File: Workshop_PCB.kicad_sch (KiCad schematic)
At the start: 15 parts, among them J1 Conn_01x04, SW1 SW_MEC_5E, U1 STM32F042C6Tx, U2 AMS1117-3.3

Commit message: Finish schematic, assign components and footprints
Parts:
- removed SW1: SW_MEC_5E, symbol Switch:SW_MEC_5E
- added D2: LED, LED_SMD:LED_0805_2012Metric, symbol Device:LED
- added J2: USB_C_Receptacle_USB2.0_16P, Connector_USB:USB_C_Receptacle_GCT_USB4105-xx-A_16P_TopMnt_Horizontal, symbol Connector:USB_C_Receptacle_USB2.0_16P
- added J3, J4: Conn_01x22, Connector_PinSocket_2.54mm:PinSocket_1x22_P2.54mm_Vertical, symbol Connector_Generic:Conn_01x22
- added R3, R4: 5.1k, Resistor_SMD:R_0603_1608Metric, symbol Device:R
- added R5: 50R, Resistor_SMD:R_0603_1608Metric, symbol Device:R
- added SW1: SW_Push, Button_Switch_SMD:SW_Push_1P1T_XKB_TS-1187A, symbol Switch:SW_Push
- added U3: USBLC6-2SC6, Package_TO_SOT_SMD:SOT-23-6, symbol Power_Protection:USBLC6-2SC6
- C1, C2, C3, C4, C5, C6, C7, C8: footprint (none) -> Capacitor_SMD:C_0603_1608Metric
- D1: footprint (none) -> LED_SMD:LED_0805_2012Metric; LCSC (none) -> C2297
- J1: footprint (none) -> Connector_PinSocket_2.54mm:PinSocket_1x04_P2.54mm_Horizontal
- R1: footprint (none) -> Resistor_SMD:R_0603_1608Metric
- R2: value R -> 220R; footprint (none) -> Resistor_SMD:R_0603_1608Metric
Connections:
- net +3V3: now also J3.5 (Pin_5)
- net +5V: now also J2.A4 (VBUS), J2.A9 (VBUS), J2.B4 (VBUS), J2.B9 (VBUS), J3.21 (Pin_21), J3.22 (Pin_22), U3.5 (VBUS)
- net A0: now also J3.7 (Pin_7)
- net A1: now also J3.8 (Pin_8)
- net A2: now also J3.9 (Pin_9)
- net A3: now also J3.10 (Pin_10)
- net A4: now also J3.11 (Pin_11)
- net A5: now also J3.12 (Pin_12)
- net A6: now also J3.13 (Pin_13)
- net A7: now also J3.14 (Pin_14)
- net A8: now also J3.15 (Pin_15)
- net A9: now also J3.16 (Pin_16)
- net BOOT: now also J3.19 (Pin_19)
- net CAN_RX_PWM_D18: now also J4.2 (Pin_2)
- net CAN_TX_PWM_D19: now also J4.1 (Pin_1)
- net D16: now also J4.4 (Pin_4)
- net D17: now also J4.3 (Pin_3)
- net D2: now also J4.20 (Pin_20)
- net D20: now also J3.1 (Pin_1)
- net D21: now also J3.2 (Pin_2)
- net D22: now also J3.3 (Pin_3)
- net D23: now also J3.4 (Pin_4)
- net D24: now also D2.2 (A)
- net D5: now also J4.17 (Pin_17)
- net D6: now also J4.16 (Pin_16)
- net D7: now also J4.14 (Pin_14)
- net D8: now also J4.13 (Pin_13)
- net GND: now also J2.A1 (GND), J2.A12 (GND), J2.B1 (GND), J2.B12 (GND), J2.S1 (SHIELD), J3.17 (Pin_17), J3.18 (Pin_18), R3.1, R4.1, R5.2, SW1.1, U3.2 (GND)
- net I2C_SCL_PWM_D3: now also J4.19 (Pin_19)
- net I2C_SDA_PWM_D4: now also J4.18 (Pin_18)
- net I2S_WS_PWM_D12: now also J4.9 (Pin_9)
- net PWM_D9: now also J4.12 (Pin_12)
- net SPI_MISO_I2S_MCK_PWM_D14: now also J4.6 (Pin_6)
- net SPI_MOSI_I2S_SD_PWM_D15: now also J4.5 (Pin_5)
- net SPI_SCK_PWM_D13: now also J4.8 (Pin_8)
- net USART_TX_PWM_D10: now also J4.11 (Pin_11)
- net USART_TX_PWM_D11: now also J4.10 (Pin_10)
- net USB_DM_D0: now also J4.22 (Pin_22), U3.6 (I/O1)
- net USB_DP_D1: now also J4.21 (Pin_21), U3.4 (I/O2)
- net NRST: now reaches C1.2, U1.7 (NRST)
- net NRST: now also J3.20 (Pin_20), SW1.2
- new net: D2.1 (K), R5.1
- new net: J2.B5 (CC2), R4.2
- new net: J2.A5 (CC1), R3.2
- new net: J2.A6 (D+), J2.B6 (D+), U3.3 (I/O2)
- new net: J2.A7 (D-), J2.B7 (D-), U3.1 (I/O1)
- no-connect marks 0 -> 5
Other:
- title: (none) -> Hackpill
- moved on the sheet: C1, C2, C3, C4, C5, C6, C7, C8, J1, R1, U1, U2

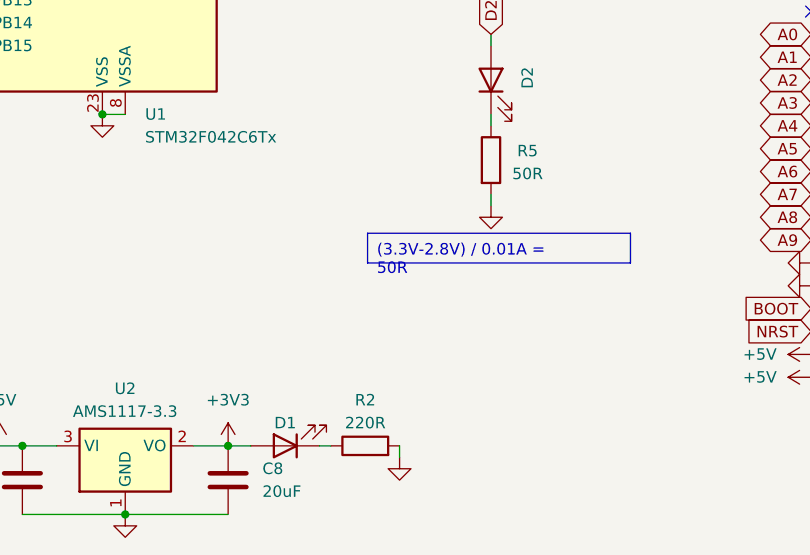
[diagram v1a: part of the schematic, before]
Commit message: Finish component selection and footprint assignment
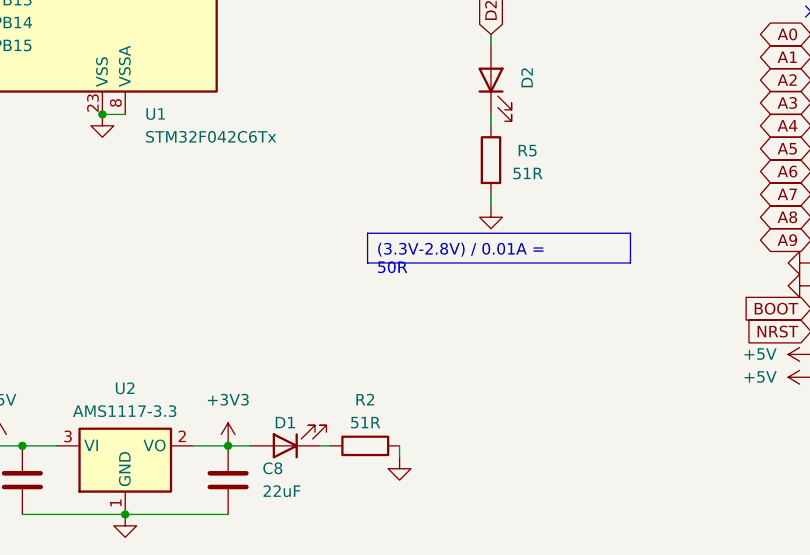
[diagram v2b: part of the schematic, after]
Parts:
- C8: value 20uF -> 22uF
- J2: footprint Connector_USB:USB_C_Receptacle_GCT_USB4105-xx-A_16P_TopMnt_Horizontal -> Connector_USB:USB_C_Receptacle_Hanbo_16P_TopMnt_Horizontal; LCSC (none) -> C6332269
- R2: value 220R -> 51R
- R5: value 50R -> 51R
- SW1: LCSC (none) -> C318884
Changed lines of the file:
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@@
 			)
 		)
-		(property "Value" "20uF"
+		(property "Value" "22uF"
 			(at 115.57 163.8299 0)
 			(effects
@@
 			)
 		)
-		(property "Footprint" "Connector_USB:USB_C_Receptacle_GCT_USB4105-xx-A_16P_TopMnt_Horizontal"
+		(property "Footprint" "Connector_USB:USB_C_Receptacle_Hanbo_16P_TopMnt_Horizontal"
 			(at 203.2 60.96 0)
 			(effects
@@
 			)
 		)
+		(property "LCSC" "C6332269"
+			(at 199.39 60.96 0)
+			(effects
+				(font
+					(size 1.27 1.27)
+				)
+				(hide yes)
+			)
+		)
 		(pin "B7"
 		)
@@
 		)
 		(property "Description" "Push button switch, generic, two pins"
+			(at 64.77 50.8 0)
+			(effects
+				(font
+					(size 1.27 1.27)
+				)
+				(hide yes)
+			)
+		)
+		(property "LCSC" "C318884"
 			(at 64.77 50.8 0)
 			(effects
@@
 			)
 		)
-		(property "Value" "220R"
+		(property "Value" "51R"
 			(at 127 156.21 90)
 			(effects
@@
 			)
 		)
-		(property "Value" "50R"
+		(property "Value" "51R"
 			(at 145.034 128.524 0)
 			(effects

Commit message: Start tracing board
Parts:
- J1: footprint Connector_PinSocket_2.54mm:PinSocket_1x04_P2.54mm_Horizontal -> Connector_PinSocket_2.54mm:PinSocket_1x04_P2.54mm_Vertical
- J3, J4: LCSC C2765186 -> (none)
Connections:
- net A0: now also U1.10 (PA0); no longer U1.19 (PB1)
- net A1: now also U1.11 (PA1); no longer U1.18 (PB0)
- net A2: now also U1.12 (PA2); no longer U1.17 (PA7)
- net A3: now also U1.13 (PA3); no longer U1.16 (PA6)
- net A4: now also U1.14 (PA4); no longer U1.15 (PA5)
- net A5: now also U1.15 (PA5); no longer U1.14 (PA4)
- net A6: now also U1.16 (PA6); no longer U1.13 (PA3)
- net A7: now also U1.17 (PA7); no longer U1.12 (PA2)
- net A8: now also U1.18 (PB0); no longer U1.11 (PA1)
- net A9: now also U1.19 (PB1); no longer U1.10 (PA0)
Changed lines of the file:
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@@
 		)
 	)
-	(global_label "A8"
+	(global_label "A1"
 		(shape bidirectional)
 		(at 113.03 53.34 0)
@@
 		)
 	)
-	(global_label "A6"
+	(global_label "A3"
 		(shape bidirectional)
 		(at 113.03 58.42 0)
@@
 		)
 	)
-	(global_label "A2"
+	(global_label "A7"
 		(shape bidirectional)
 		(at 113.03 68.58 0)
@@
 		)
 	)
-	(global_label "A5"
+	(global_label "A4"
 		(shape bidirectional)
 		(at 113.03 60.96 0)
@@
 		)
 	)
-	(global_label "A9"
+	(global_label "A0"
 		(shape bidirectional)
 		(at 113.03 50.8 0)
@@
 		)
 	)
-	(global_label "A1"
+	(global_label "A8"
 		(shape bidirectional)
 		(at 82.55 76.2 180)
@@
 		)
 	)
-	(global_label "A3"
+	(global_label "A6"
 		(shape bidirectional)
 		(at 113.03 66.04 0)
@@
 		)
 	)
-	(global_label "A4"
+	(global_label "A5"
 		(shape bidirectional)
 		(at 113.03 63.5 0)
@@
 		)
 	)
-	(global_label "A0"
+	(global_label "A9"
 		(shape bidirectional)
 		(at 82.55 78.74 180)
@@
 		)
 	)
-	(global_label "A7"
+	(global_label "A2"
 		(shape bidirectional)
 		(at 113.03 55.88 0)
@@
 			)
 		)
-		(property "Footprint" "Connector_PinSocket_2.54mm:PinSocket_1x04_P2.54mm_Horizontal"
+		(property "Footprint" "Connector_PinSocket_2.54mm:PinSocket_1x04_P2.54mm_Vertical"
 			(at 142.24 83.82 0)
 			(effects
@@
 			)
 		)
-		(property "LCSC" "C2765186"
+		(property "LCSC" ""
 			(at 186.69 123.19 0)
 			(effects
@@
 			)
 		)
-		(property "LCSC" "C2765186"
+		(property "LCSC" ""
 			(at 181.61 123.19 0)
 			(effects

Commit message: Finish PCB
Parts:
- J1: footprint Connector_PinSocket_2.54mm:PinSocket_1x04_P2.54mm_Vertical -> Connector_PinHeader_2.54mm:PinHeader_1x04_P2.54mm_Vertical
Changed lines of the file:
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@@
 			)
 		)
-		(property "Footprint" "Connector_PinSocket_2.54mm:PinSocket_1x04_P2.54mm_Vertical"
+		(property "Footprint" "Connector_PinHeader_2.54mm:PinHeader_1x04_P2.54mm_Vertical"
 			(at 142.24 83.82 0)
 			(effects

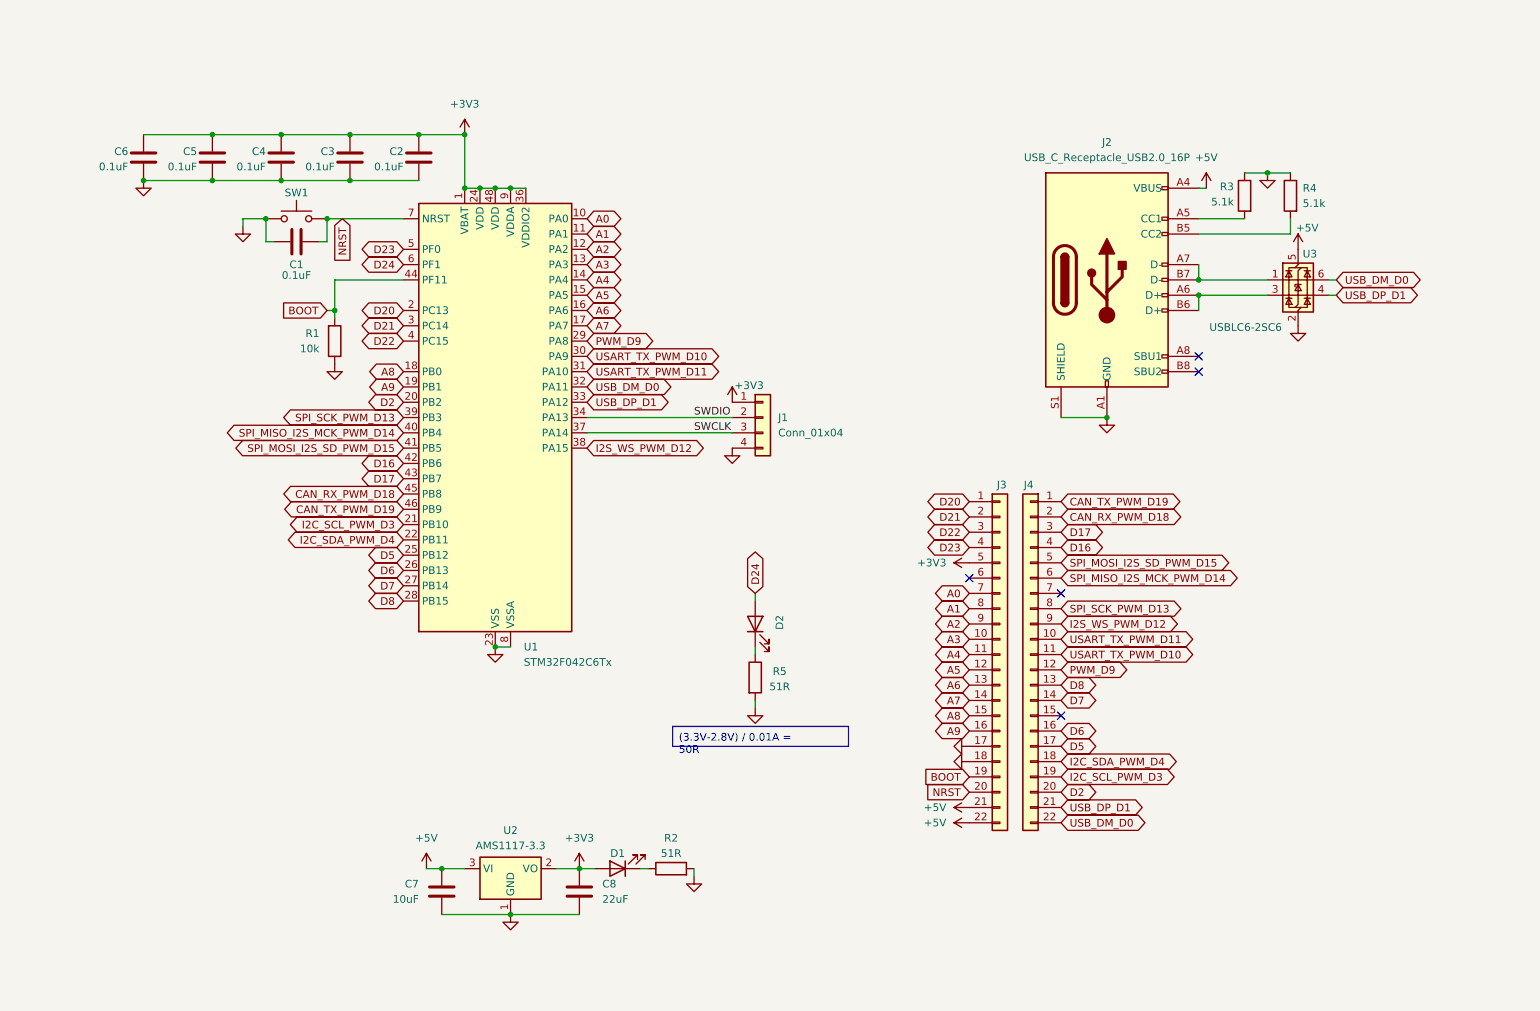
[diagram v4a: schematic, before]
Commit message: Adjust trace width, adjust pinout, make changes to schematic
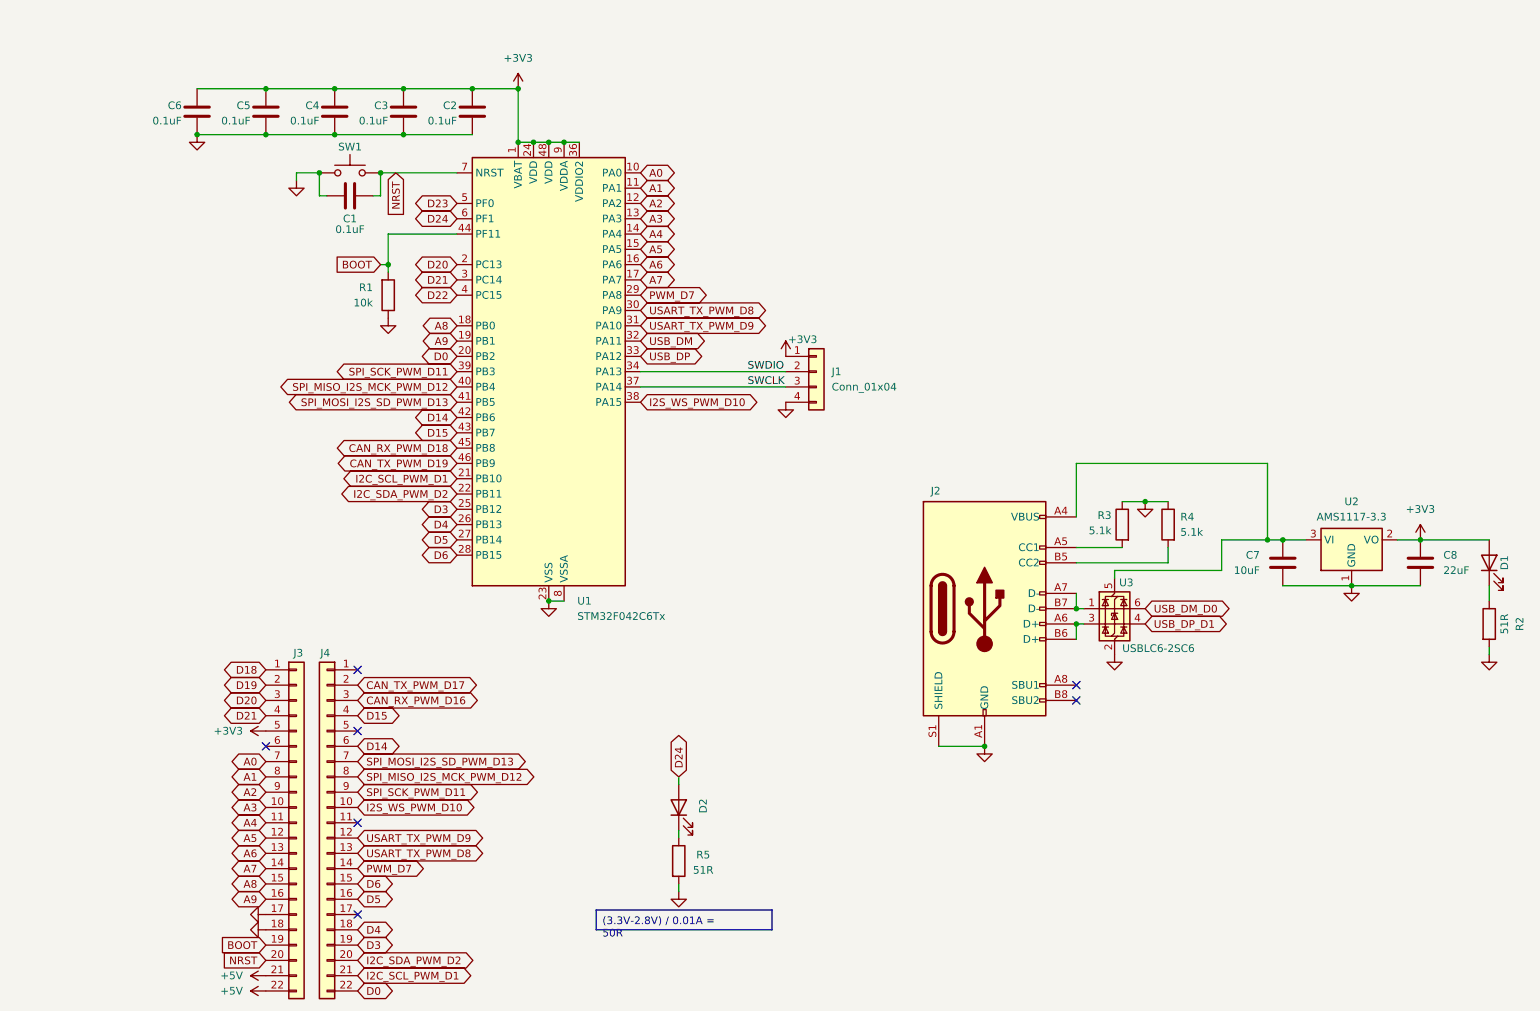
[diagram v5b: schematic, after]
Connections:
- net +5V: no longer C7.1, J2.A4 (VBUS), J2.A9 (VBUS), J2.B4 (VBUS), J2.B9 (VBUS), U2.3 (VI), U3.5 (VBUS)
- net CAN_RX_PWM_D18: no longer J4.2 (Pin_2)
- net CAN_TX_PWM_D19: no longer J4.1 (Pin_1)
- net D20: now also J3.3 (Pin_3); no longer J3.1 (Pin_1)
- net D21: now also J3.4 (Pin_4); no longer J3.2 (Pin_2)
- net D22: no longer J3.3 (Pin_3)
- net D23: no longer J3.4 (Pin_4)
- net D5: now also J4.16 (Pin_16), U1.27 (PB14); no longer J4.17 (Pin_17), U1.25 (PB12)
- net D6: now also J4.15 (Pin_15), U1.28 (PB15); no longer J4.16 (Pin_16), U1.26 (PB13)
- net USB_DM_D0: no longer J4.22 (Pin_22), U1.32 (PA11)
- net USB_DP_D1: no longer J4.21 (Pin_21), U1.33 (PA12)
- net SPI_MOSI_I2S_SD_PWM_D13: now reaches J4.7 (Pin_7)
- net SPI_MOSI_I2S_SD_PWM_D13: now also U1.41 (PB5)
- net D16 renamed D14
- net D14: now also J4.6 (Pin_6); no longer J4.4 (Pin_4)
- net D17 renamed CAN_RX_PWM_D16
- net CAN_RX_PWM_D16: no longer U1.43 (PB7)
- net D2 renamed D0
- net D0: now also J4.22 (Pin_22); no longer J4.20 (Pin_20)
- net D7 renamed PWM_D7
- net PWM_D7: now also U1.29 (PA8); no longer U1.27 (PB14)
- net D8 renamed USART_TX_PWM_D8
- net USART_TX_PWM_D8: now also U1.30 (PA9); no longer U1.28 (PB15)
- net I2C_SCL_PWM_D3 renamed D3
- net D3: now also U1.25 (PB12); no longer U1.21 (PB10)
- net I2C_SDA_PWM_D4 renamed D4
- net D4: now also U1.26 (PB13); no longer U1.22 (PB11)
- net I2S_WS_PWM_D12 renamed I2S_WS_PWM_D10
- net I2S_WS_PWM_D10: now also J4.10 (Pin_10); no longer J4.9 (Pin_9)
- net PWM_D9 renamed USART_TX_PWM_D9
- net USART_TX_PWM_D9: now also U1.31 (PA10); no longer U1.29 (PA8)
- net SPI_MISO_I2S_MCK_PWM_D14 renamed SPI_MISO_I2S_MCK_PWM_D12
- net SPI_MISO_I2S_MCK_PWM_D12: now also J4.8 (Pin_8); no longer J4.6 (Pin_6)
- net SPI_MOSI_I2S_SD_PWM_D15: no longer names the net of J4.5 (Pin_5)
- net SPI_MOSI_I2S_SD_PWM_D15: no longer U1.41 (PB5)
- net SPI_SCK_PWM_D13 renamed SPI_SCK_PWM_D11
- net SPI_SCK_PWM_D11: now also J4.9 (Pin_9); no longer J4.8 (Pin_8)
- net USART_TX_PWM_D10: no longer names the net of J4.11 (Pin_11)
- net USART_TX_PWM_D10: no longer U1.30 (PA9)
- removed net USART_TX_PWM_D11: J4.10 (Pin_10), U1.31 (PA10)
- new net: C7.1, J2.A4 (VBUS), J2.A9 (VBUS), J2.B4 (VBUS), J2.B9 (VBUS), U2.3 (VI), U3.5 (VBUS)
- new net CAN_TX_PWM_D17: J4.2 (Pin_2)
- new net D15: J4.4 (Pin_4), U1.43 (PB7)
- new net D18: J3.1 (Pin_1)
- new net D19: J3.2 (Pin_2)
- new net I2C_SCL_PWM_D1: J4.21 (Pin_21), U1.21 (PB10)
- new net I2C_SDA_PWM_D2: J4.20 (Pin_20), U1.22 (PB11)
- new net USB_DM: U1.32 (PA11)
- new net USB_DP: U1.33 (PA12)
- no-connect marks 5 -> 7
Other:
- moved on the sheet: C1, C2, C3, C4, C5, C6, C7, C8, D1, D2, J1, J2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
